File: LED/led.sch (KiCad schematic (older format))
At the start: 4 parts

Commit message: Finish LED scematics
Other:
- moved on the sheet: C1, LED
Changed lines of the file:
@@
 L Connector:Conn_01x03_Male J?
 U 1 1 607A4CB2
-P 1300 2050
-F 0 "J?" H 1408 2331 50  0001 C CNN
-F 1 "Conn_01x03_Male" H 1408 2240 50  0001 C CNN
-F 2 "" H 1300 2050 50  0001 C CNN
-F 3 "~" H 1300 2050 50  0001 C CNN
-	1    1300 2050
+P 4100 3950
+F 0 "J?" H 4208 4231 50  0001 C CNN
+F 1 "Conn_01x03_Male" H 4208 4140 50  0001 C CNN
+F 2 "" H 4100 3950 50  0001 C CNN
+F 3 "~" H 4100 3950 50  0001 C CNN
+	1    4100 3950
 	1    0    0    -1
 $EndComp
 Wire Wire Line
-	1500 2050 2500 2050
+	4300 3950 5300 3950
 Wire Wire Line
-	2500 2050 2500 2200
+	5300 3950 5300 4100
 $Comp
 L Connector:Conn_01x03_Male J?
 U 1 1 607A2A3A
-P 4700 2050
-F 0 "J?" H 4672 2074 50  0001 R CNN
-F 1 "Conn_01x03_Male" H 4672 1983 50  0001 R CNN
-F 2 "" H 4700 2050 50  0001 C CNN
-F 3 "~" H 4700 2050 50  0001 C CNN
-	1    4700 2050
+P 7500 3950
+F 0 "J?" H 7472 3974 50  0001 R CNN
+F 1 "Conn_01x03_Male" H 7472 3883 50  0001 R CNN
+F 2 "" H 7500 3950 50  0001 C CNN
+F 3 "~" H 7500 3950 50  0001 C CNN
+	1    7500 3950
 	-1   0    0    -1
 $EndComp
 Wire Wire Line
-	3500 2050 4500 2050
-Text GLabel 1300 1950 0    50   Input ~ 0
-GND
-Text GLabel 1300 2050 0    50   Input ~ 0
-DATA
-Text GLabel 4700 2050 2    50   Output ~ 0
-DATA
-Text GLabel 4700 2150 2    50   Output ~ 0
-5V
-Text GLabel 1300 2150 0    50   Input ~ 0
-5V
+	6300 3950 7300 3950
 Wire Wire Line
-	3500 1800 3500 2050
+	6300 3700 6300 3950
 $Comp
 L ws2812b:WS2812B LED
 U 1 1 6079C2AE
-P 3000 2000
-F 0 "LED" H 2947 2362 60  0000 L CNN
-F 1 "WS2812B" H 3150 2362 60  0000 L CNN
-F 2 "" V 2950 2000 60  0000 C CNN
-F 3 "" V 2950 2000 60  0000 C CNN
-	1    3000 2000
+P 5800 3900
+F 0 "LED" H 5747 4262 60  0000 L CNN
+F 1 "WS2812B" H 5950 4262 60  0000 L CNN
+F 2 "" V 5750 3900 60  0000 C CNN
+F 3 "" V 5750 3900 60  0000 C CNN
+	1    5800 3900
 	-1   0    0    1
 $EndComp
 Wire Wire Line
-	1500 1100 2500 1100
+	4300 3000 5300 3000
 Wire Wire Line
-	1500 2900 3500 2900
-Connection ~ 2500 1100
+	4300 4800 6300 4800
+Connection ~ 5300 3000
 Wire Wire Line
-	2500 1100 4500 1100
-Connection ~ 3500 2900
+	5300 3000 7300 3000
+Connection ~ 6300 4800
 Wire Wire Line
-	3500 2900 4500 2900
+	6300 4800 7300 4800
 Wire Wire Line
-	4500 2150 4500 2900
+	7300 4050 7300 4800
 Wire Wire Line
-	1500 2150 1500 2900
+	4300 4050 4300 4800
 Wire Wire Line
-	1500 1100 1500 1950
+	4300 3000 4300 3850
 Wire Wire Line
-	4500 1100 4500 1950
+	7300 3000 7300 3850
 Wire Wire Line
-	3500 2200 3500 2400
+	6300 4100 6300 4300
 Wire Wire Line
-	2500 1800 2500 1100
+	5300 3700 5300 3000
 $Comp
 L Device:C C1
 U 1 1 607F11E7
-P 3500 2550
-F 0 "C1" H 3615 2596 50  0000 L CNN
-F 1 "100 - 1000 uF" H 3615 2505 50  0000 L CNN
-F 2 "" H 3538 2400 50  0001 C CNN
-F 3 "~" H 3500 2550 50  0001 C CNN
-	1    3500 2550
+P 6300 4450
+F 0 "C1" H 6415 4496 50  0000 L CNN
+F 1 "100 - 1000 uF" H 6415 4405 50  0000 L CNN
+F 2 "" H 6338 4300 50  0001 C CNN
+F 3 "~" H 6300 4450 50  0001 C CNN
+	1    6300 4450
 	1    0    0    -1
 $EndComp
 Wire Wire Line
-	3500 2700 3500 2900
-Text Notes 2650 900  0    118  ~ 0
+	6300 4600 6300 4800
+Text Notes 5450 2800 0    118  ~ 0
 LED PCB
-Text GLabel 4700 1950 2    50   Output ~ 0
+Text Label 4100 3850 2    50   ~ 0
 GND
+Text Label 4100 3950 2    50   ~ 0
+DATA
+Text Label 4100 4050 2    50   ~ 0
+5V
+Text Label 7500 3850 0    50   ~ 0
+GND
+Text Label 7500 3950 0    50   ~ 0
+DATA
+Text Label 7500 4050 0    50   ~ 0
+5V
 $EndSCHEMATC

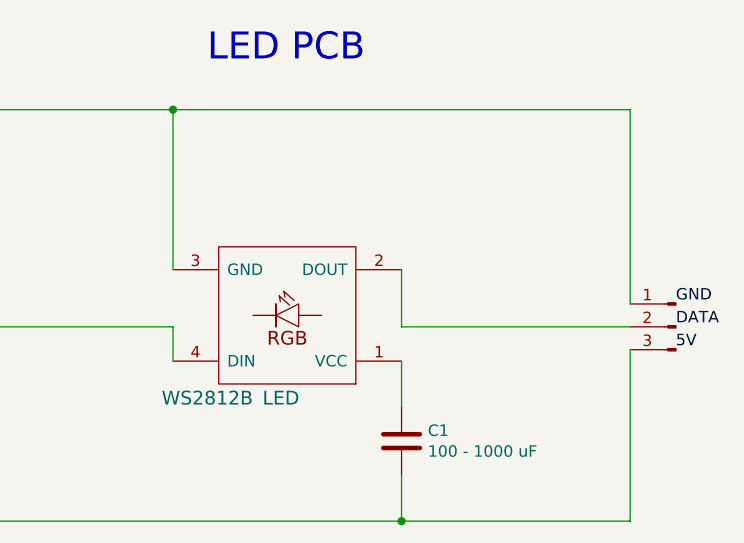
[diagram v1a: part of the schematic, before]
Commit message: Fix minor mistakes after the presentation
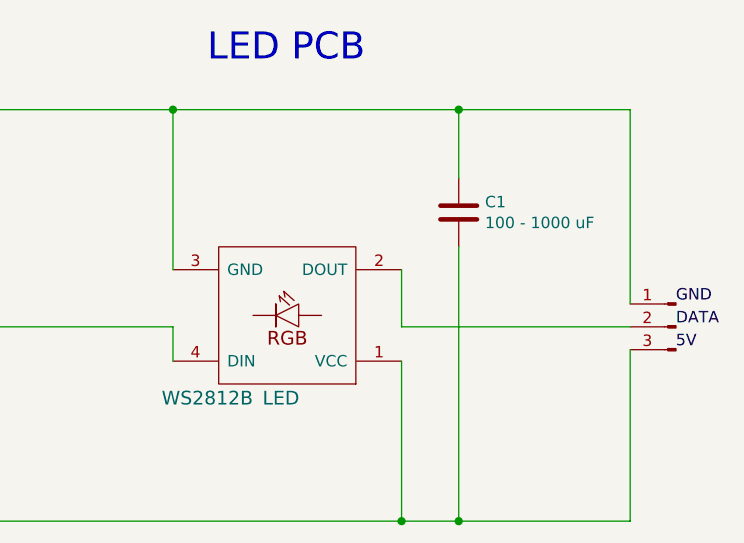
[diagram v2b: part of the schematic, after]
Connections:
- net at LED.1 (VCC): now also C1.2, J?.3 (Pin_3), J?.3 (Pin_3); no longer C1.1
- net at J?.1 (Pin_1), J?.1 (Pin_1), LED.3 (GND): now also C1.1
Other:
- moved on the sheet: C1
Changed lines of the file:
@@
 Connection ~ 5300 3000
 Wire Wire Line
-	5300 3000 7300 3000
+	5300 3000 6550 3000
 Connection ~ 6300 4800
-Wire Wire Line
-	6300 4800 7300 4800
 Wire Wire Line
 	7300 4050 7300 4800
@@
 	7300 3000 7300 3850
 Wire Wire Line
-	6300 4100 6300 4300
-Wire Wire Line
 	5300 3700 5300 3000
 $Comp
 L Device:C C1
 U 1 1 607F11E7
-P 6300 4450
-F 0 "C1" H 6415 4496 50  0000 L CNN
-F 1 "100 - 1000 uF" H 6415 4405 50  0000 L CNN
-F 2 "" H 6338 4300 50  0001 C CNN
-F 3 "~" H 6300 4450 50  0001 C CNN
-	1    6300 4450
+P 6550 3450
+F 0 "C1" H 6665 3496 50  0000 L CNN
+F 1 "100 - 1000 uF" H 6665 3405 50  0000 L CNN
+F 2 "" H 6588 3300 50  0001 C CNN
+F 3 "~" H 6550 3450 50  0001 C CNN
+	1    6550 3450
 	1    0    0    -1
 $EndComp
-Wire Wire Line
-	6300 4600 6300 4800
 Text Notes 5450 2800 0    118  ~ 0
 LED PCB
@@
 Text Label 7500 4050 0    50   ~ 0
 5V
+Wire Wire Line
+	6300 4100 6300 4800
+Wire Wire Line
+	6550 3600 6550 4800
+Wire Wire Line
+	6300 4800 6550 4800
+Connection ~ 6550 4800
+Wire Wire Line
+	6550 4800 7300 4800
+Wire Wire Line
+	6550 3300 6550 3000
+Connection ~ 6550 3000
+Wire Wire Line
+	6550 3000 7300 3000
 $EndSCHEMATC

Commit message: hub pcb stuck
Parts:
- C1: footprint (none) -> Capacitor_SMD:C_0603_1608Metric
- J1, J2: renamed from J?; footprint (none) -> Connector_Wire:SolderWire-0.1sqmm_1x03_P3.6mm_D0.4mm_OD1mm
- LED1: renamed from LED; footprint (none) -> LED_SMD:LED_WS2812B_PLCC4_5.0x5.0mm_P3.2mm
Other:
- moved on the sheet: C1, LED1
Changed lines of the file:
@@
 $EndDescr
 $Comp
-L Connector:Conn_01x03_Male J?
+L Connector:Conn_01x03_Male J1
 U 1 1 607A4CB2
-P 4100 3950
-F 0 "J?" H 4208 4231 50  0001 C CNN
-F 1 "Conn_01x03_Male" H 4208 4140 50  0001 C CNN
-F 2 "" H 4100 3950 50  0001 C CNN
-F 3 "~" H 4100 3950 50  0001 C CNN
-	1    4100 3950
+P 4200 3600
+F 0 "J1" H 4308 3881 50  0001 C CNN
+F 1 "Conn_01x03_Male" H 4308 3790 50  0001 C CNN
+F 2 "Connector_Wire:SolderWire-0.1sqmm_1x03_P3.6mm_D0.4mm_OD1mm" H 4200 3600 50  0001 C CNN
+F 3 "~" H 4200 3600 50  0001 C CNN
+	1    4200 3600
 	1    0    0    -1
 $EndComp
 Wire Wire Line
-	4300 3950 5300 3950
+	4400 3600 5400 3600
 Wire Wire Line
-	5300 3950 5300 4100
+	5400 3600 5400 3750
 $Comp
-L Connector:Conn_01x03_Male J?
+L Connector:Conn_01x03_Male J2
 U 1 1 607A2A3A
-P 7500 3950
-F 0 "J?" H 7472 3974 50  0001 R CNN
-F 1 "Conn_01x03_Male" H 7472 3883 50  0001 R CNN
-F 2 "" H 7500 3950 50  0001 C CNN
-F 3 "~" H 7500 3950 50  0001 C CNN
-	1    7500 3950
+P 7600 3600
+F 0 "J2" H 7572 3624 50  0001 R CNN
+F 1 "Conn_01x03_Male" H 7572 3533 50  0001 R CNN
+F 2 "Connector_Wire:SolderWire-0.1sqmm_1x03_P3.6mm_D0.4mm_OD1mm" H 7600 3600 50  0001 C CNN
+F 3 "~" H 7600 3600 50  0001 C CNN
+	1    7600 3600
 	-1   0    0    -1
 $EndComp
 Wire Wire Line
-	6300 3950 7300 3950
+	6400 3600 7400 3600
 Wire Wire Line
-	6300 3700 6300 3950
+	6400 3350 6400 3600
 $Comp
-L ws2812b:WS2812B LED
+L ws2812b:WS2812B LED1
 U 1 1 6079C2AE
-P 5800 3900
-F 0 "LED" H 5747 4262 60  0000 L CNN
-F 1 "WS2812B" H 5950 4262 60  0000 L CNN
-F 2 "" V 5750 3900 60  0000 C CNN
-F 3 "" V 5750 3900 60  0000 C CNN
-	1    5800 3900
+P 5900 3550
+F 0 "LED1" H 5847 3912 60  0000 L CNN
+F 1 "WS2812B" H 6050 3912 60  0000 L CNN
+F 2 "LED_SMD:LED_WS2812B_PLCC4_5.0x5.0mm_P3.2mm" V 5850 3550 60  0001 C CNN
+F 3 "" V 5850 3550 60  0000 C CNN
+	1    5900 3550
 	-1   0    0    1
 $EndComp
 Wire Wire Line
-	4300 3000 5300 3000
+	4400 2650 5400 2650
 Wire Wire Line
-	4300 4800 6300 4800
-Connection ~ 5300 3000
+	4400 4450 6400 4450
+Connection ~ 5400 2650
 Wire Wire Line
-	5300 3000 6550 3000
-Connection ~ 6300 4800
+	5400 2650 6650 2650
+Connection ~ 6400 4450
 Wire Wire Line
-	7300 4050 7300 4800
+	7400 3700 7400 4450
 Wire Wire Line
-	4300 4050 4300 4800
+	4400 3700 4400 4450
 Wire Wire Line
-	4300 3000 4300 3850
+	4400 2650 4400 3500
 Wire Wire Line
-	7300 3000 7300 3850
+	7400 2650 7400 3500
 Wire Wire Line
-	5300 3700 5300 3000
+	5400 3350 5400 2650
 $Comp
 L Device:C C1
 U 1 1 607F11E7
-P 6550 3450
-F 0 "C1" H 6665 3496 50  0000 L CNN
-F 1 "100 - 1000 uF" H 6665 3405 50  0000 L CNN
-F 2 "" H 6588 3300 50  0001 C CNN
-F 3 "~" H 6550 3450 50  0001 C CNN
-	1    6550 3450
+P 6650 3100
+F 0 "C1" H 6765 3146 50  0000 L CNN
+F 1 "100 - 1000 uF" H 6765 3055 50  0000 L CNN
+F 2 "Capacitor_SMD:C_0603_1608Metric" H 6688 2950 50  0001 C CNN
+F 3 "~" H 6650 3100 50  0001 C CNN
+	1    6650 3100
 	1    0    0    -1
 $EndComp
-Text Notes 5450 2800 0    118  ~ 0
+Text Notes 5550 2450 0    118  ~ 0
 LED PCB
-Text Label 4100 3850 2    50   ~ 0
+Text Label 4200 3500 2    50   ~ 0
 GND
-Text Label 4100 3950 2    50   ~ 0
+Text Label 4200 3600 2    50   ~ 0
 DATA
-Text Label 4100 4050 2    50   ~ 0
+Text Label 4200 3700 2    50   ~ 0
 5V
-Text Label 7500 3850 0    50   ~ 0
+Text Label 7600 3500 0    50   ~ 0
 GND
-Text Label 7500 3950 0    50   ~ 0
+Text Label 7600 3600 0    50   ~ 0
 DATA
-Text Label 7500 4050 0    50   ~ 0
+Text Label 7600 3700 0    50   ~ 0
 5V
 Wire Wire Line
-	6300 4100 6300 4800
+	6400 3750 6400 4450
 Wire Wire Line
-	6550 3600 6550 4800
+	6650 3250 6650 4450
 Wire Wire Line
-	6300 4800 6550 4800
-Connection ~ 6550 4800
+	6400 4450 6650 4450
+Connection ~ 6650 4450
 Wire Wire Line
-	6550 4800 7300 4800
+	6650 4450 7400 4450
 Wire Wire Line
-	6550 3300 6550 3000
-Connection ~ 6550 3000
+	6650 2950 6650 2650
+Connection ~ 6650 2650
 Wire Wire Line
-	6550 3000 7300 3000
+	6650 2650 7400 2650
 $EndSCHEMATC
